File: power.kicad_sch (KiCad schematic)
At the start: 39 parts, among them J1 Battery 1, J7 Battery 2, J8 USB, U1 AMS1117-3.3, U5 TPS62933, U6 TPS62933

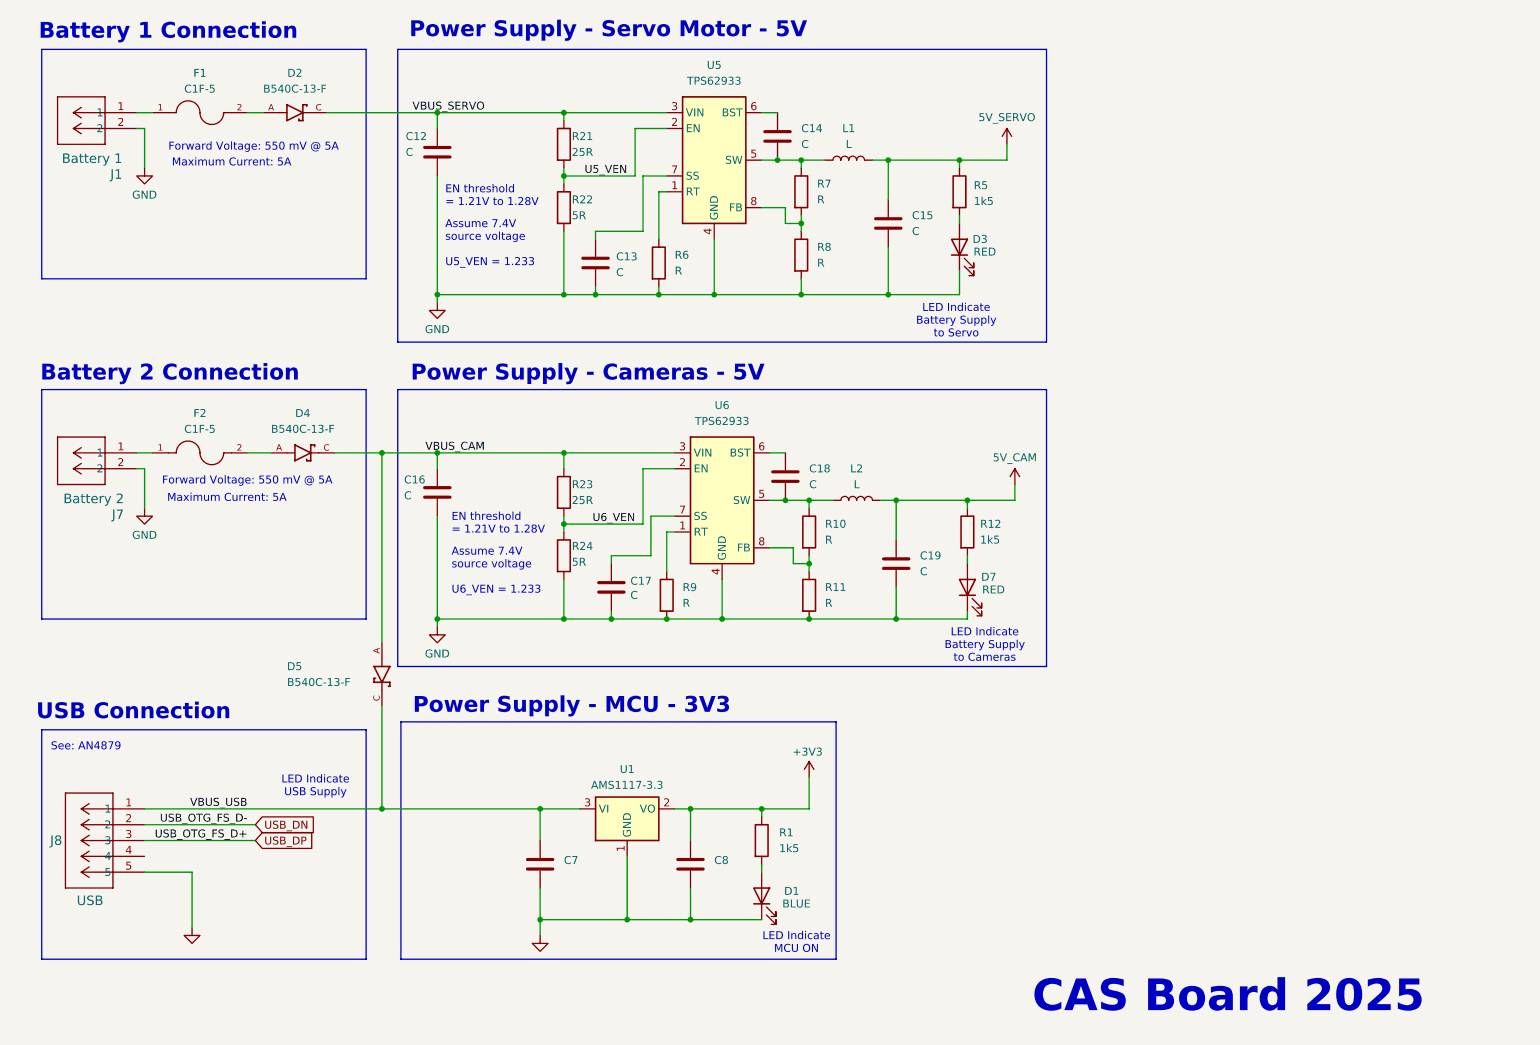
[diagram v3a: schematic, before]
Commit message: Add net names to power
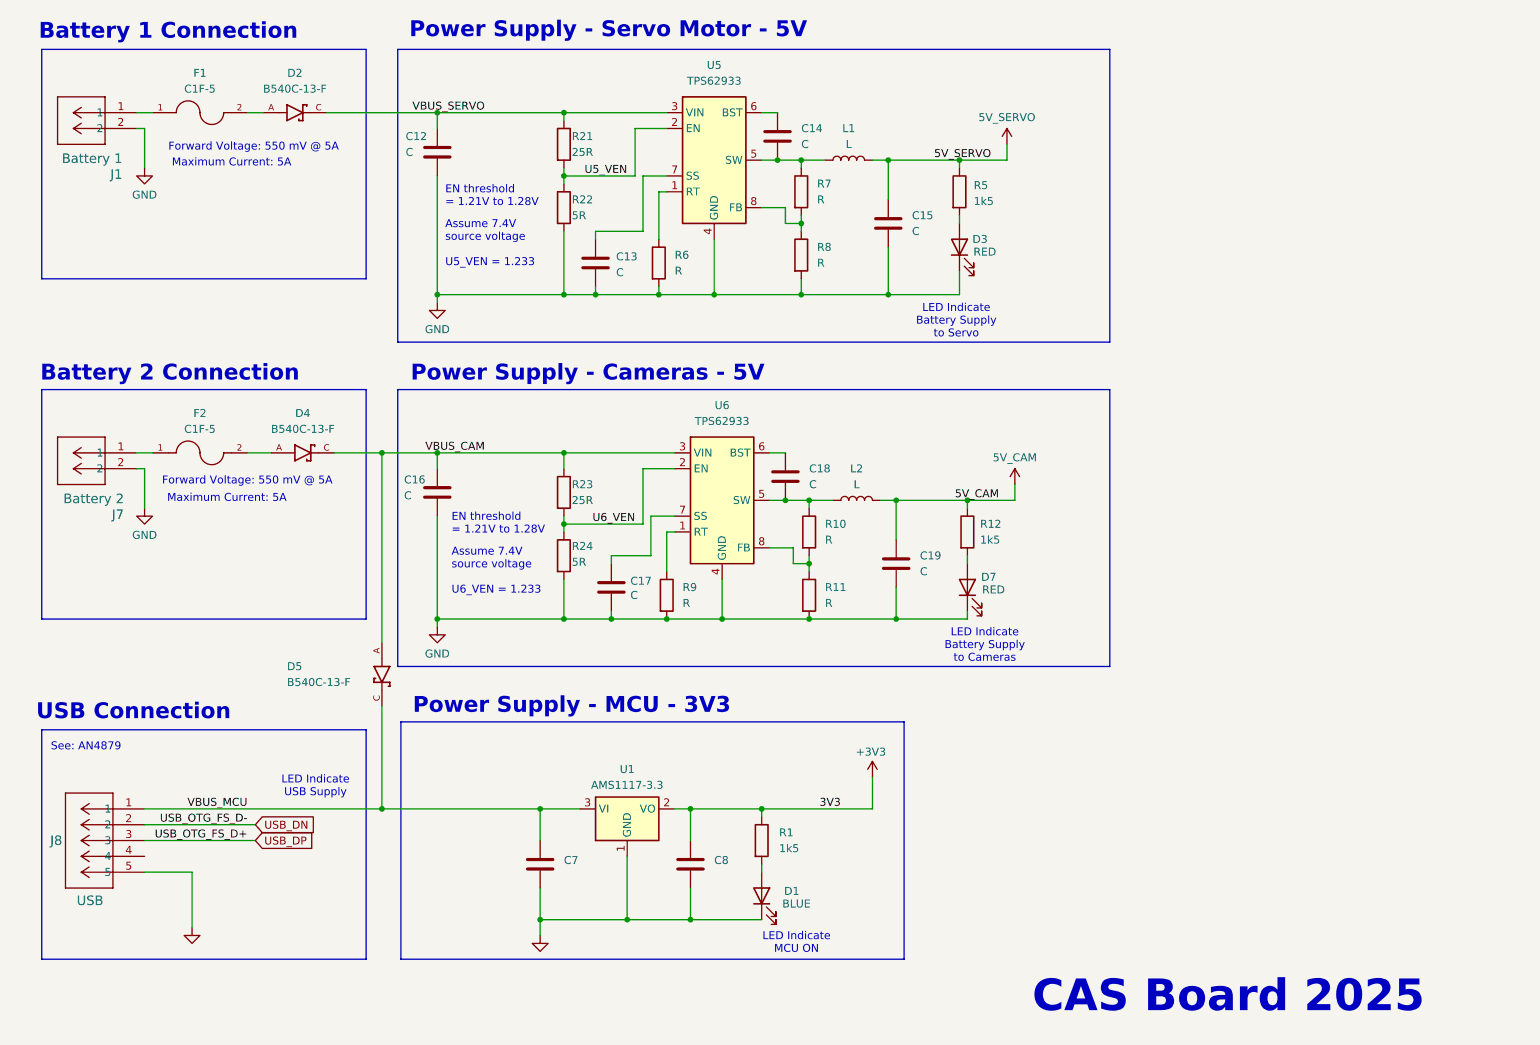
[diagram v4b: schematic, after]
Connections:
- net VBUS_USB renamed VBUS_MCU
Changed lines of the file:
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@@
 	(polyline
 		(pts
-			(xy 76.2 76.2) (xy 180.34 76.2)
+			(xy 76.2 76.2) (xy 190.5 76.2)
 		)
 		(stroke
@@
 	(wire
 		(pts
-			(xy 142.24 138.43) (xy 142.24 143.51)
+			(xy 152.4 138.43) (xy 152.4 143.51)
 		)
 		(stroke
@@
 	(polyline
 		(pts
-			(xy 180.34 68.58) (xy 76.2 68.58)
+			(xy 190.5 68.58) (xy 76.2 68.58)
 		)
 		(stroke
@@
 	(polyline
 		(pts
-			(xy 180.34 76.2) (xy 180.34 120.65)
+			(xy 190.5 76.2) (xy 190.5 120.65)
 		)
 		(stroke
@@
 	(polyline
 		(pts
-			(xy 76.708 129.54) (xy 146.558 129.54)
+			(xy 76.708 129.54) (xy 157.48 129.54)
 		)
 		(stroke
@@
 	(polyline
 		(pts
-			(xy 180.34 120.65) (xy 76.2 120.65)
+			(xy 190.5 120.65) (xy 76.2 120.65)
 		)
 		(stroke
@@
 	(wire
 		(pts
-			(xy 142.24 143.51) (xy 134.62 143.51)
+			(xy 152.4 143.51) (xy 134.62 143.51)
 		)
 		(stroke
@@
 	(polyline
 		(pts
-			(xy 76.2 21.59) (xy 180.34 21.59)
+			(xy 76.2 21.59) (xy 190.5 21.59)
 		)
 		(stroke
@@
 	(polyline
 		(pts
-			(xy 146.558 129.54) (xy 146.558 167.64)
+			(xy 157.48 129.54) (xy 157.48 167.64)
 		)
 		(stroke
@@
 	(polyline
 		(pts
-			(xy 180.34 21.59) (xy 180.34 68.58)
+			(xy 190.5 21.59) (xy 190.5 68.58)
 		)
 		(stroke
@@
 	(polyline
 		(pts
-			(xy 146.558 167.64) (xy 76.708 167.64)
+			(xy 157.48 167.64) (xy 76.708 167.64)
 		)
 		(stroke
@@
 		)
 	)
-	(label "VBUS_USB"
+	(label "VBUS_MCU"
 		(at 52.07 143.51 180)
 		(effects
@@
 		)
 	)
+	(label "5V_SERVO"
+		(at 171.45 39.37 180)
+		(effects
+			(font
+				(size 1.27 1.27)
+			)
+			(justify right bottom)
+		)
+	)
 	(label "VBUS_SERVO"
 		(at 90.17 31.75 180)
@@
 		)
 	)
+	(label "3V3"
+		(at 147.32 143.51 180)
+		(effects
+			(font
+				(size 1.27 1.27)
+			)
+			(justify right bottom)
+		)
+	)
 	(label "USB_OTG_FS_D+"
 		(at 52.07 148.59 180)
@@
 		)
 	)
+	(label "5V_CAM"
+		(at 172.72 93.98 180)
+		(effects
+			(font
+				(size 1.27 1.27)
+			)
+			(justify right bottom)
+		)
+	)
 	(label "USB_OTG_FS_D-"
 		(at 52.07 146.05 180)
@@
 	(symbol
 		(lib_id "power:+3V3")
-		(at 142.24 138.43 0)
+		(at 152.4 138.43 0)
 		(unit 1)
 		(exclude_from_sim no)
@@
 		(dnp no)
 		(property "Reference" "#PWR03"
-			(at 142.24 142.24 0)
+			(at 152.4 142.24 0)
 			(effects
 				(font
@@
 		)
 		(property "Value" "+3V3"
-			(at 141.986 134.366 0)
+			(at 152.146 134.366 0)
 			(effects
 				(font
@@
 		)
 		(property "Footprint" ""
-			(at 142.24 138.43 0)
+			(at 152.4 138.43 0)
 			(effects
 				(font
@@
 		)
 		(property "Datasheet" ""
-			(at 142.24 138.43 0)
+			(at 152.4 138.43 0)
 			(effects
 				(font
@@
 		)
 		(property "Description" "Power symbol creates a global label with name \"+3V3\""
-			(at 142.24 138.43 0)
+			(at 152.4 138.43 0)
 			(effects
 				(font

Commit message: Use heirarchical labels
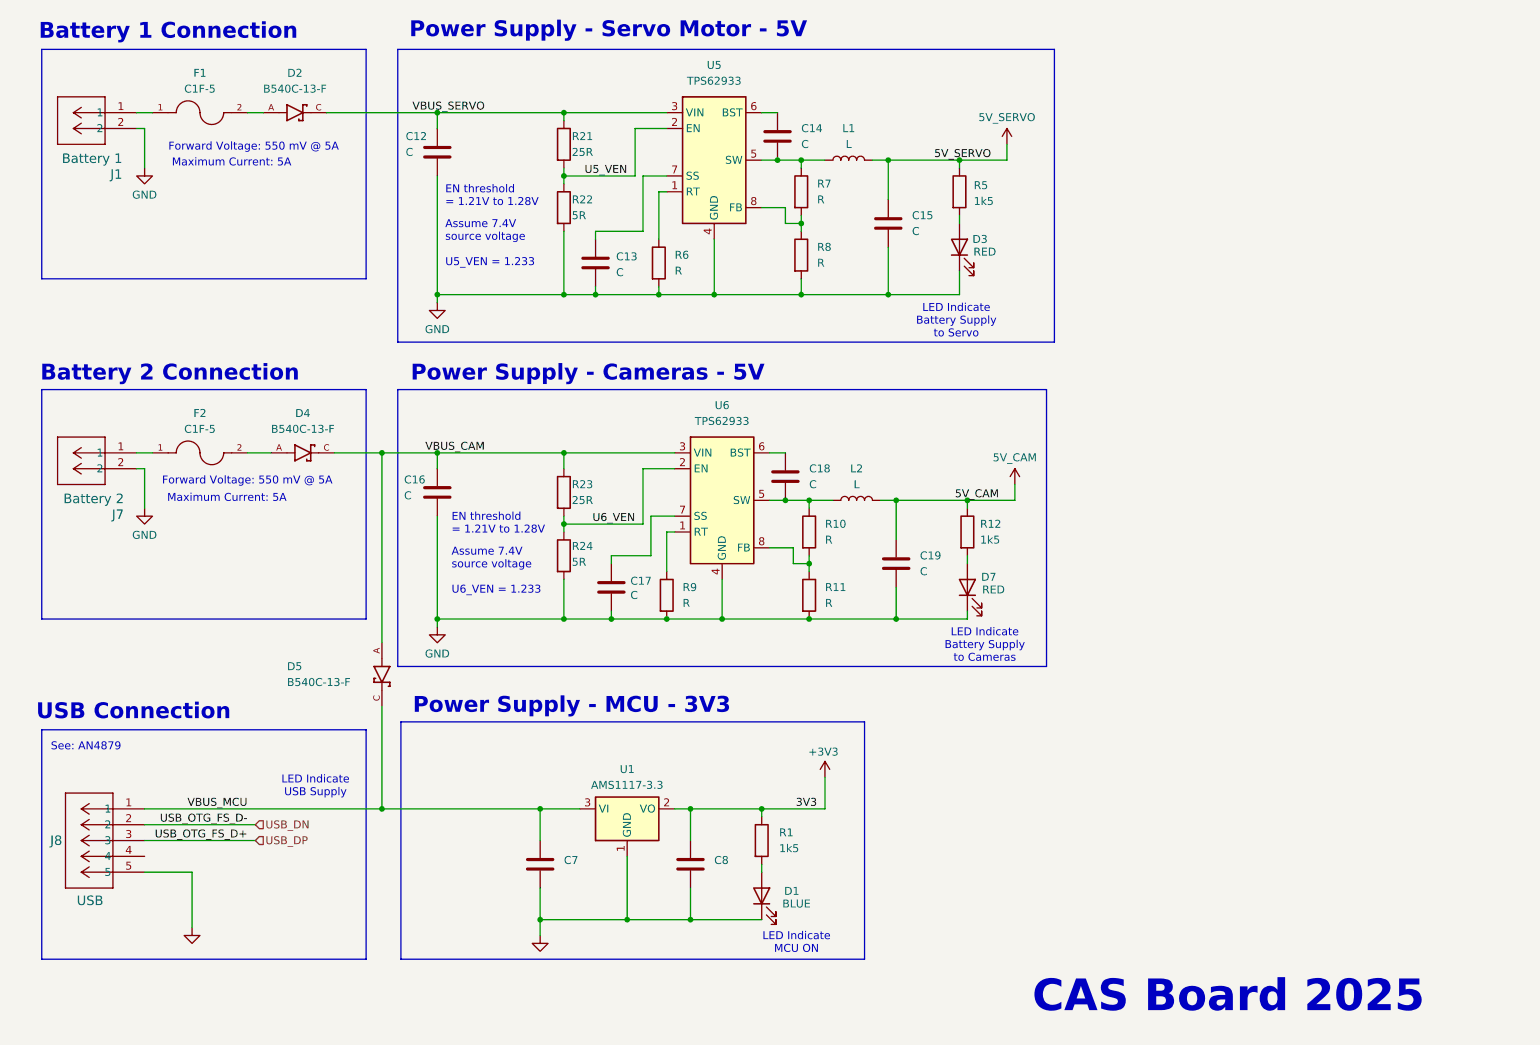
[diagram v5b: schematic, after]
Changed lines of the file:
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@@
 	(polyline
 		(pts
-			(xy 76.2 76.2) (xy 190.5 76.2)
+			(xy 76.2 76.2) (xy 180.34 76.2)
 		)
 		(stroke
@@
 	(wire
 		(pts
-			(xy 152.4 138.43) (xy 152.4 143.51)
+			(xy 144.78 143.51) (xy 144.78 138.43)
 		)
 		(stroke
@@
 	(polyline
 		(pts
-			(xy 190.5 68.58) (xy 76.2 68.58)
+			(xy 181.61 68.58) (xy 76.2 68.58)
 		)
 		(stroke
@@
 	(polyline
 		(pts
-			(xy 190.5 76.2) (xy 190.5 120.65)
+			(xy 180.34 76.2) (xy 180.34 120.65)
 		)
 		(stroke
@@
 	(polyline
 		(pts
-			(xy 76.708 129.54) (xy 157.48 129.54)
+			(xy 76.708 129.54) (xy 151.13 129.54)
 		)
 		(stroke
@@
 	(polyline
 		(pts
-			(xy 190.5 120.65) (xy 76.2 120.65)
+			(xy 180.34 120.65) (xy 76.2 120.65)
 		)
 		(stroke
@@
 	(wire
 		(pts
-			(xy 152.4 143.51) (xy 134.62 143.51)
+			(xy 134.62 143.51) (xy 144.78 143.51)
 		)
 		(stroke
@@
 	(polyline
 		(pts
-			(xy 76.2 21.59) (xy 190.5 21.59)
+			(xy 76.2 21.59) (xy 181.61 21.59)
 		)
 		(stroke
@@
 	(polyline
 		(pts
-			(xy 157.48 129.54) (xy 157.48 167.64)
+			(xy 151.13 129.54) (xy 151.13 167.64)
 		)
 		(stroke
@@
 	(polyline
 		(pts
-			(xy 190.5 21.59) (xy 190.5 68.58)
+			(xy 181.61 21.59) (xy 181.61 68.58)
 		)
 		(stroke
@@
 	(polyline
 		(pts
-			(xy 157.48 167.64) (xy 76.708 167.64)
+			(xy 151.13 167.64) (xy 76.708 167.64)
 		)
 		(stroke
@@
 	)
 	(label "3V3"
-		(at 147.32 143.51 180)
+		(at 143.51 143.51 180)
 		(effects
 			(font
@@
 		)
 	)
-	(global_label "USB_DP"
+	(hierarchical_label "USB_DN"
 		(shape input)
-		(at 53.34 148.59 0)
-		(fields_autoplaced yes)
+		(at 53.34 146.05 0)
 		(effects
 			(font
@@
 			(justify left)
 		)
-		(property "Intersheetrefs" "${INTERSHEET_REFS}"
-			(at 63.6428 148.59 0)
-			(effects
-				(font
-					(size 1.27 1.27)
-				)
-				(justify left)
-			)
-		)
 	)
-	(global_label "USB_DN"
+	(hierarchical_label "USB_DP"
 		(shape input)
-		(at 53.34 146.05 0)
-		(fields_autoplaced yes)
+		(at 53.34 148.59 0)
 		(effects
 			(font
@@
 			(justify left)
 		)
-		(property "Intersheetrefs" "${INTERSHEET_REFS}"
-			(at 63.7033 146.05 0)
-			(effects
-				(font
-					(size 1.27 1.27)
-				)
-				(justify left)
-			)
-		)
 	)
 	(symbol
@@
 	(symbol
 		(lib_id "power:+3V3")
-		(at 152.4 138.43 0)
+		(at 144.78 138.43 0)
 		(unit 1)
 		(exclude_from_sim no)
@@
 		(dnp no)
 		(property "Reference" "#PWR03"
-			(at 152.4 142.24 0)
+			(at 144.78 142.24 0)
 			(effects
 				(font
@@
 		)
 		(property "Value" "+3V3"
-			(at 152.146 134.366 0)
+			(at 144.526 134.366 0)
 			(effects
 				(font
@@
 		)
 		(property "Footprint" ""
-			(at 152.4 138.43 0)
+			(at 144.78 138.43 0)
 			(effects
 				(font
@@
 		)
 		(property "Datasheet" ""
-			(at 152.4 138.43 0)
+			(at 144.78 138.43 0)
 			(effects
 				(font
@@
 		)
 		(property "Description" "Power symbol creates a global label with name \"+3V3\""
-			(at 152.4 138.43 0)
+			(at 144.78 138.43 0)
 			(effects
 				(font
